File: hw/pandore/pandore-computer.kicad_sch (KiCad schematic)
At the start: 1 part

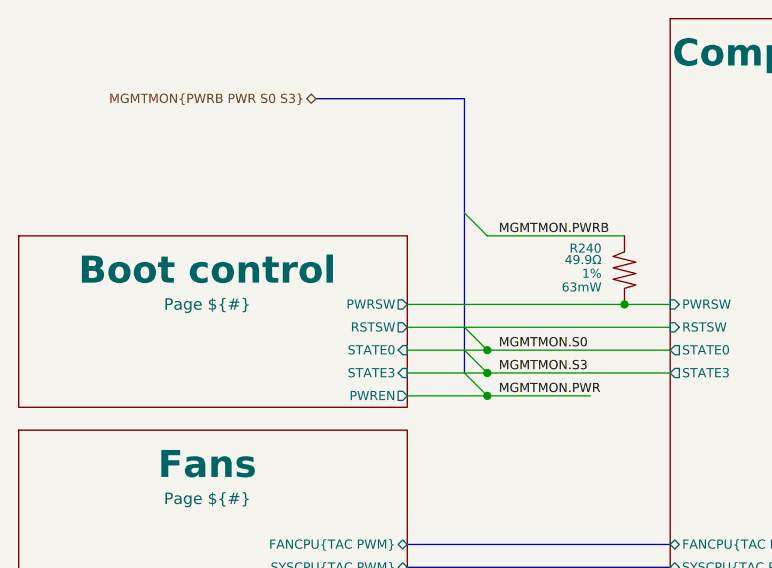
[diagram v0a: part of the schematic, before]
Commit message: added monitor amp with volume knob continue routing all around
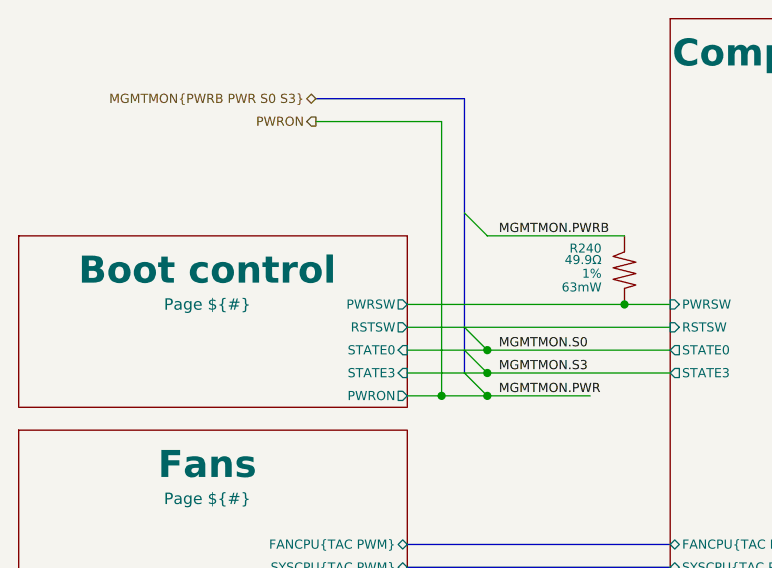
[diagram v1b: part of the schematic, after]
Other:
- sheet Boot control ports: added PWRON; removed PWREN
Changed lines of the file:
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@@
+	)
+	(junction
+		(at 96.52 74.93)
+		(diameter 0)
+		(color 0 0 0 0)
 	)
 	(junction
@@
 		)
 	)
+	(wire
+		(pts
+			(xy 82.55 44.45) (xy 96.52 44.45)
+		)
+		(stroke
+			(width 0)
+			(type default)
+		)
+	)
 	(bus
 		(pts
@@
 	(wire
 		(pts
-			(xy 92.71 74.93) (xy 101.6 74.93)
+			(xy 92.71 74.93) (xy 96.52 74.93)
 		)
 		(stroke
@@
 		)
 	)
+	(wire
+		(pts
+			(xy 96.52 74.93) (xy 101.6 74.93)
+		)
+		(stroke
+			(width 0)
+			(type default)
+		)
+	)
 	(bus
 		(pts
@@
 		(pts
 			(xy 165.1 64.77) (xy 201.93 64.77)
+		)
+		(stroke
+			(width 0)
+			(type default)
+		)
+	)
+	(wire
+		(pts
+			(xy 96.52 44.45) (xy 96.52 74.93)
 		)
 		(stroke
@@
 			)
 			(justify left)
+		)
+	)
+	(hierarchical_label "PWRON"
+		(shape output)
+		(at 82.55 44.45 180)
+		(effects
+			(font
+				(size 1.016 1.016)
+			)
+			(justify right)
 		)
 	)
@@
 			)
 		)
-		(pin "PWREN" output
+		(pin "PWRON" output
 			(at 92.71 74.93 0)
 			(effects

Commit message: last sprint almost done, most routing done
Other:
- sheet Computer module ports: added none; removed SUSCLK
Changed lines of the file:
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@@
-	(wire
-		(pts
-			(xy 165.1 82.55) (xy 215.9 82.55)
-		)
-		(stroke
-			(width 0)
-			(type default)
-		)
-	)
 	(wire
 		(pts
@@
 		(shape bidirectional)
 		(at 215.9 119.38 0)
-		(effects
-			(font
-				(size 1.016 1.016)
-			)
-			(justify left)
-		)
-	)
-	(hierarchical_label "SUSCLK"
-		(shape output)
-		(at 215.9 82.55 0)
 		(effects
 			(font
@@
 			)
 		)
-		(pin "SUSCLK" output
-			(at 165.1 82.55 0)
-			(effects
-				(font
-					(size 1.016 1.016)
-				)
-				(justify right)
-			)
-		)

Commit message: all routed, review starting
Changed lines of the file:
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@@
+		)
+	)
+	(wire
+		(pts
+			(xy 165.1 107.95) (xy 215.9 107.95)
+		)
+		(stroke
+			(width 0)
+			(type default)
 		)
 	)
@@
 		(pts
 			(xy 92.71 74.93) (xy 96.52 74.93)
+		)
+		(stroke
+			(width 0)
+			(type default)
+		)
+	)
+	(wire
+		(pts
+			(xy 92.71 144.78) (xy 121.92 144.78)
 		)
 		(stroke
@@
 		)
 	)
+	(hierarchical_label "AUDIO.EN"
+		(shape output)
+		(at 92.71 144.78 180)
+		(effects
+			(font
+				(size 1.016 1.016)
+			)
+			(justify right)
+		)
+	)
 	(hierarchical_label "M2E{USB2}"
 		(shape bidirectional)
@@
 		(shape bidirectional)
 		(at 215.9 100.33 0)
+		(effects
+			(font
+				(size 1.016 1.016)
+			)
+			(justify left)
+		)
+	)
+	(hierarchical_label "VUSB.EN"
+		(shape output)
+		(at 215.9 107.95 0)
 		(effects
 			(font
@@
 		)
 		(pin "GPP_F12" bidirectional
-			(at 144.78 175.26 270)
+			(at 121.92 144.78 180)
 			(effects
 				(font
@@
 		)
 		(pin "GPP_D0" bidirectional
-			(at 138.43 175.26 270)
-			(effects
-				(font
-					(size 1.016 1.016)
-				)
-				(justify left)
-			)
-		)
+			(at 165.1 107.95 0)
+			(effects
+				(font
+					(size 1.016 1.016)
+				)
+				(justify right)
+			)
+		)

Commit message: finished adding mpn,mfg to all parts, finished routing placement
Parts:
- R240: Link (none) -> https://yageogroup.com/products/Resistors/part/RC0402FR-074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; MFG (none) -> YAGEO; MPN (none) -> RC0402FR-0749R9L
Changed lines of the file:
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@@
 			)
 		)
-		(property "Datasheet" ""
+		(property "Datasheet" "https://yageogroup.com/content/datasheet/asset/file/PYU-RC_GROUP_51_ROHS_L"
 			(at 116.84 46.736 0)
 			(do_not_autoplace yes)
@@
 			)
 		)
-		(property "MPN" ""
+		(property "MPN" "RC0402FR-0749R9L"
 			(at 116.84 43.18 0)
 			(do_not_autoplace yes)
@@
 			)
 		)
-		(property "MFG" ""
+		(property "MFG" "YAGEO"
 			(at 102.87 43.434 0)
 			(do_not_autoplace yes)
@@
 			)
 		)
-		(property "Link" ""
+		(property "Link" "https://yageogroup.com/products/Resistors/part/RC0402FR-0749R9L"
 			(at 73.025 43.18 0)
 			(do_not_autoplace yes)
